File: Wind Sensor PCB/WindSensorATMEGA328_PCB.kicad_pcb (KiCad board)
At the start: 2 copper layers, 44.9 x 44.9 mm, 33 parts, among them P1 I2C, P10 I2C, P2 SERIAL, P3 ID, P4 ISP, P5 LOGO2, P6 PCB, P8 ADC, P9 PROG, SW1 SWA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

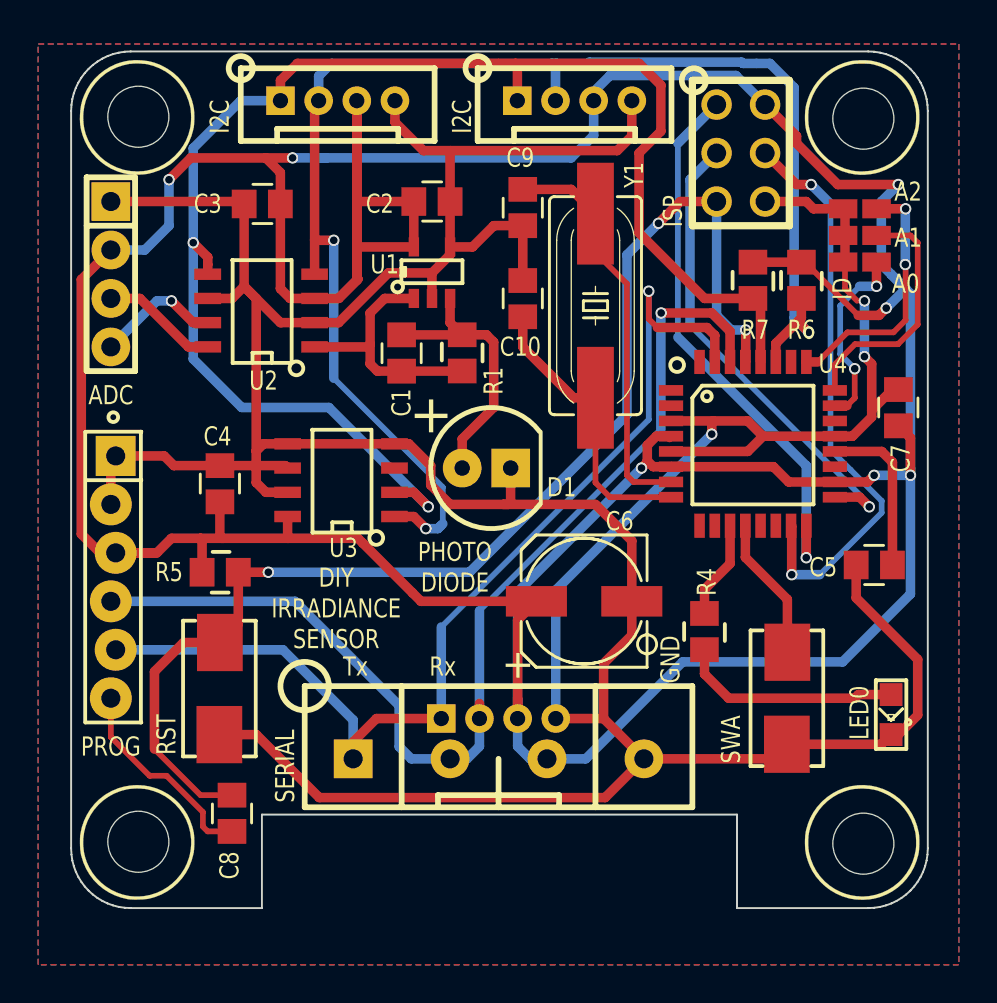
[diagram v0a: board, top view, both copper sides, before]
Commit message: Updated PCB
Version 1 of the PCB with ATMEGA328 used...
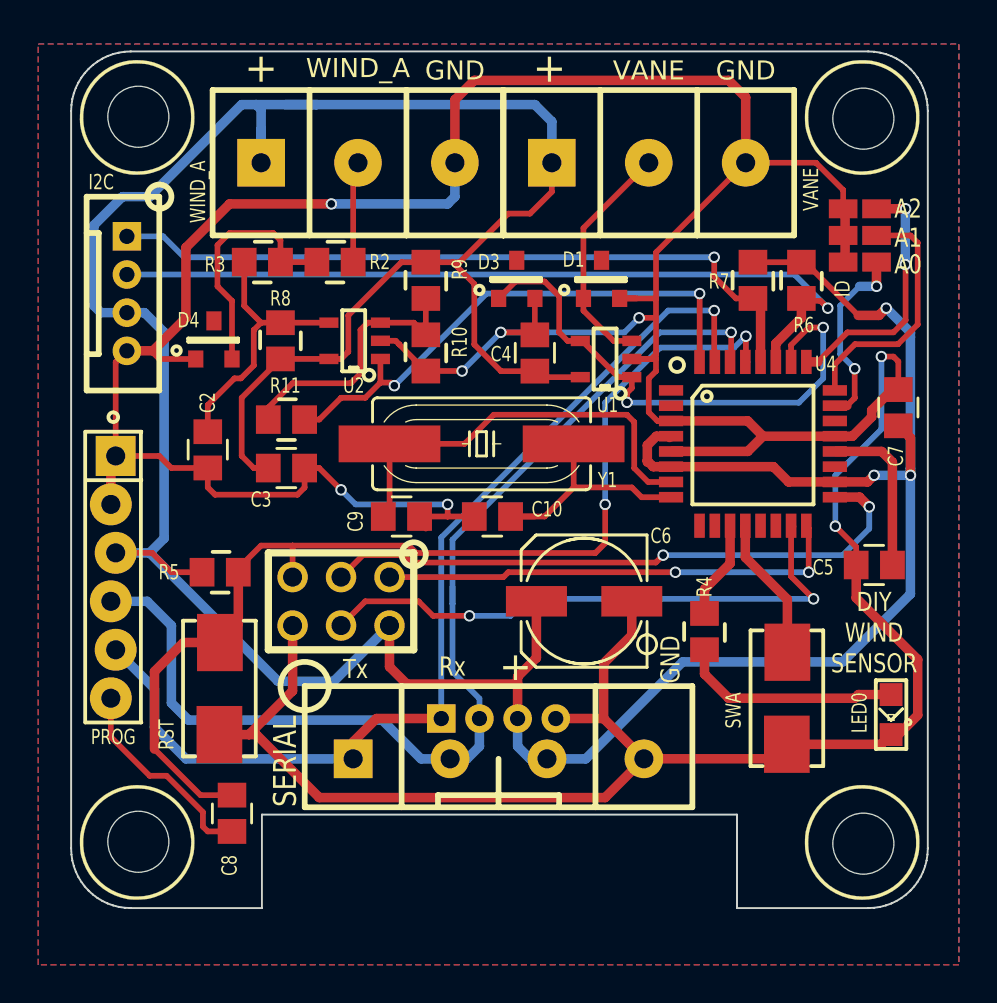
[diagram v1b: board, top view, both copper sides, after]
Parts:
- removed C1: 10n, REInnovationFootprint:SM_C_0805
- removed P1: I2C, REInnovationFootprint:SIL-4_Grove_Not_Labelled
- removed R1: 47k, REInnovationFootprint:SM0805
- removed U3: LM75B, REInnovationFootprint:SM_SOIC_8
- added D3: 5V1_Zener, REInnovationFootprint:SOT23, F.Cu at (149.5, 101.2)
- added D4: 3V3_Zener, REInnovationFootprint:SOT23, F.Cu at (133.7, 104.4)
- added P11: WIND_A, REInnovationFootprint:SIL-3_screw_terminal, F.Cu at (136.1, 95.1)
- added R10: 10k, REInnovationFootprint:SM0805, F.Cu at (144.8, 105.1)
- added R11: 4M7, REInnovationFootprint:SM0805, F.Cu at (137.5, 108.6)
- added R2: 4k7, REInnovationFootprint:SM0805, F.Cu at (140.0, 100.3)
- added R3: 4k7, REInnovationFootprint:SM0805, F.Cu at (136.2, 100.3)
- added R8: 100k, REInnovationFootprint:SM0805, F.Cu at (137.2, 104.5)
- added R9: 100k, REInnovationFootprint:SM0805, F.Cu at (144.8, 101.3)
- C2: value 100n -> 22n
- D1: value PHOTO DIODE -> 5V1_Zener; footprint REInnovationFootprint:TH_LED-5MM_larg_pad -> REInnovationFootprint:SOT23
- P8: value ADC -> VANE; footprint REInnovationFootprint:SIL-4_large_pad -> REInnovationFootprint:SIL-3_screw_terminal
- R6, R7: value 4k7 -> 10k
- U2: value MCP3426-xSN -> TSV911xxLx; footprint REInnovationFootprint:SM_SOIC_8 -> REInnovationFootprint:SM_SOT-23-5
- moved P4 31.4 mm to (139.7, 118.1), turned to 180 degrees
- moved P8 23.8 mm to (151.4, 95.1), turned to 0 degrees
- moved C4 17.9 mm to (150.5, 105.1)
- moved C2 17.5 mm to (133.3, 110.2), turned to 270 degrees
- moved C9 17.4 mm to (143.5, 113.7), turned to 180 degrees
- moved P10 15.4 mm to (127.0, 102.0), turned to 270 degrees
- moved C3 13.9 mm to (137.5, 111.1), turned to 0 degrees
- moved D1 11.6 mm to (154.0, 101.2)
- moved C10 11.5 mm to (148.3, 113.7), turned to 0 degrees
- moved U1 10.9 mm to (155.6, 105.4), turned to 90 degrees
- moved Y1 9.38 mm to (147.7, 109.9), turned to 0 degrees
- moved U2 6.63 mm to (142.4, 104.5)
- moved P5 2.96 mm to (155.3, 99.1)
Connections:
- C2 pad 1: GND -> Net-(C2-Pad1)
- C2 pad 2: VCC -> GND
- D1 pad 1: Net-(C1-Pad2) -> /Wind_Vane/WIND_V_SIG
- P8 pad 1: GND -> VCC
- P8 pad 2: VCC -> /Wind_Vane/WIND_V_SIG
- P8 pad 3: Net-(P8-Pad3) -> GND
- U1 pad 1: Net-(C1-Pad1) -> /WIND_VANE
- U1 pad 3: Net-(C1-Pad2) -> /Wind_Vane/WIND_V_SIG
- U1 pad 4: GND -> /WIND_VANE
- U2 pad 1: Net-(C1-Pad1) -> /WIND_FREQ
- U2 pad 3: VCC -> Net-(R10-Pad2)
- U2 pad 4: /I2C_SDA -> Net-(C2-Pad1)
- U2 pad 5: /I2C_CLK -> VCC
- U4 pad 26: /ATMega328/A3 -> /WIND_VANE
- U4 pad 32: /ATMega328/D2 -> /WIND_FREQ
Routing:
- net /I2C_SDA: track 89.1 -> 43.1 mm, vias 3 -> 1
- net VCC: track 246.2 -> 204.6 mm, vias 7 -> 3
- net /I2C_CLK: track 79.6 -> 38.6 mm, vias 2 -> 1
- net /WIND_VANE: track 0.00 -> 28.4 mm, vias 0 -> 2
- net /WIND_FREQ: track 0.00 -> 28.4 mm, vias 0 -> 2
- net Net-(C1-Pad2): track 14.4 -> 0.00 mm
- net Net-(R10-Pad2): track 0.00 -> 14.2 mm
- net Net-(C2-Pad1): track 0.00 -> 14.2 mm
- net Net-(C1-Pad1): track 13.2 -> 0.00 mm
- net Net-(D4-Pad2): track 0.00 -> 13.1 mm
- net GND: track 223.5 -> 236.5 mm, vias 3 -> 8
- net /Wind_Vane/WIND_V_SIG: track 0.00 -> 12.4 mm
- net /ATMega328/RESET: track 64.8 -> 56.8 mm, vias 3 -> 2
- net /ATMega328/SCLK: track 25.0 -> 32.3 mm, vias 1 -> 2
- net Net-(P8-Pad4): track 6.55 -> 0.00 mm, vias 1 -> 0
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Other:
- board text added: "DIY WIND SENSOR"
- board text removed: "DIY IRRADIANCE SENSOR"
- board text removed: "PHOTO DIODE"
- board text removed: "www.curiouselectric.co.uk"

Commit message: large code update
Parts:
- C10, C9: value 22pf -> 22p
- C5, C7, C8: value 100nf -> 100n
- C6: value 100uf -> 100u
- D1, D3, D4: footprint REInnovationFootprint:SOT23 -> REInnovationFootprint:SOT23_ZENER
- moved D1 0.63 mm to (154.6, 101.2)
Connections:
- D1 pad 1: /Wind_Vane/WIND_V_SIG -> GND
- D1 pad 2: GND -> /Wind_Vane/WIND_V_SIG
- D3 pad 1: /WIND_VANE -> GND
- D3 pad 2: GND -> /WIND_VANE
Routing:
- net /Wind_Vane/WIND_V_SIG: track 12.4 -> 14.9 mm
- net Net-(D4-Pad2): track 13.1 -> 10.8 mm
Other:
- rule pad_to_mask_clearance: 0.1 -> 0
